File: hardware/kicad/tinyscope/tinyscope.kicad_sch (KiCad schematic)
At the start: 44 parts, among them J1 USB_C_Receptacle_USB2.0, J2 Conn_01x02, J3 Conn_01x02, Q1 PMOS, U1 USBLC6-2SC6_MOD, U2 BQ24075RGT, U3 MAX17048G, U4 TPS54360DDA

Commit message: feat: hardware: Add tinyscope kicad project. Adds TPS62133 3V3 buck converter
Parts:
- added C13: 100n, symbol Device:C_Small
- added C14: 10u, symbol Device:C_Small
- added C15: 3n3, symbol Device:C_Small
- added C16: 22u, symbol Device:C_Small
- added L2: 2u2, symbol Device:L_Small
- added R16: 100k, symbol Device:R_Small
- added R17: 31k8, symbol Device:R_Small
- added R18: 10k2, symbol Device:R_Small
- added U5: TPS62133, Package_DFN_QFN:VQFN-16-1EP_3x3mm_P0.5mm_EP1.68x1.68mm_ThermalVias, symbol Regulator_Switching:TPS62133
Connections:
- net BQ24075_OUT: now also C14.1, U5.11 (PVIN), U5.12 (PVIN)
- net GND: now also C13.2, C14.2, C15.1, C16.2, R18.2, U5.15 (PGND), U5.16 (PGND), U5.17 (EP), U5.6 (AGND), U5.7 (FSW), U5.8 (DEF)
- new net: R17.2, R18.1, U5.5 (FB)
- new net: L2.1, U5.1 (SW), U5.2 (SW), U5.3 (SW)
- new net: C13.1, U5.10 (AVIN), U5.13 (EN)
- new net: L2.2, R16.1, U5.14 (VOS)
- new net: C15.2, U5.9 (SS/TR)
- new net +3V3: C16.1, R16.2, R17.1, U5.4 (PG)

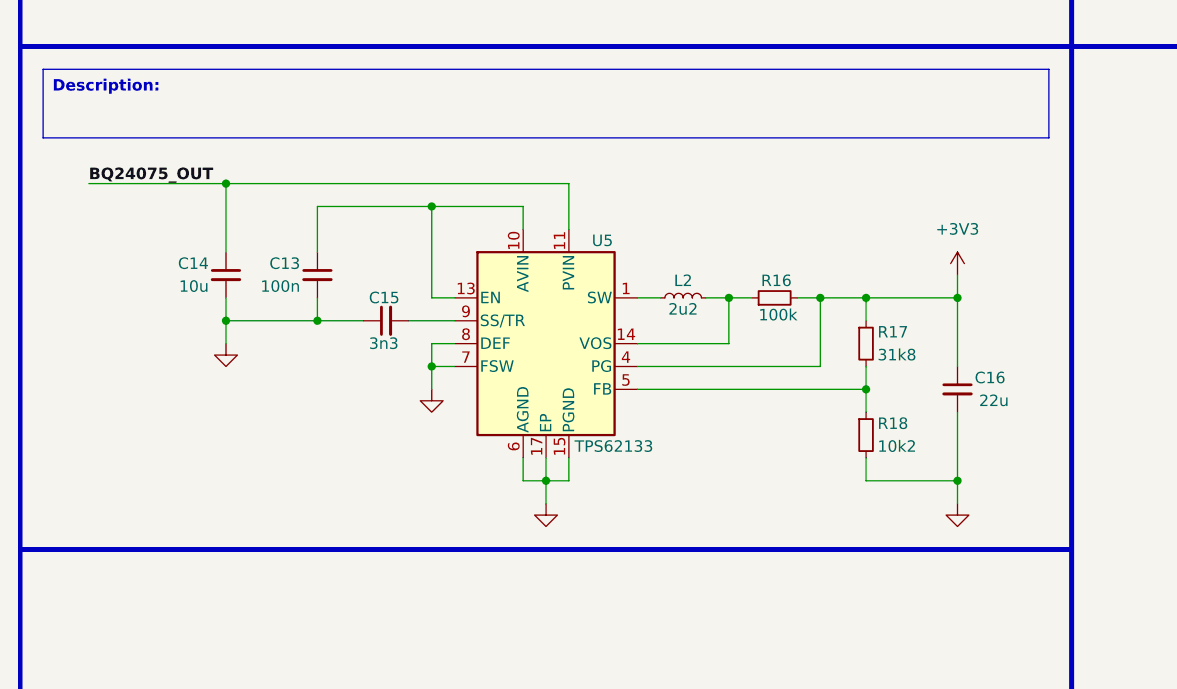
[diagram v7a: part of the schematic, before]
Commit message: feat: hardware: Add tinyscope kicad project. Adds TPS63802 3V3 buck-boost converter instead of the previous one
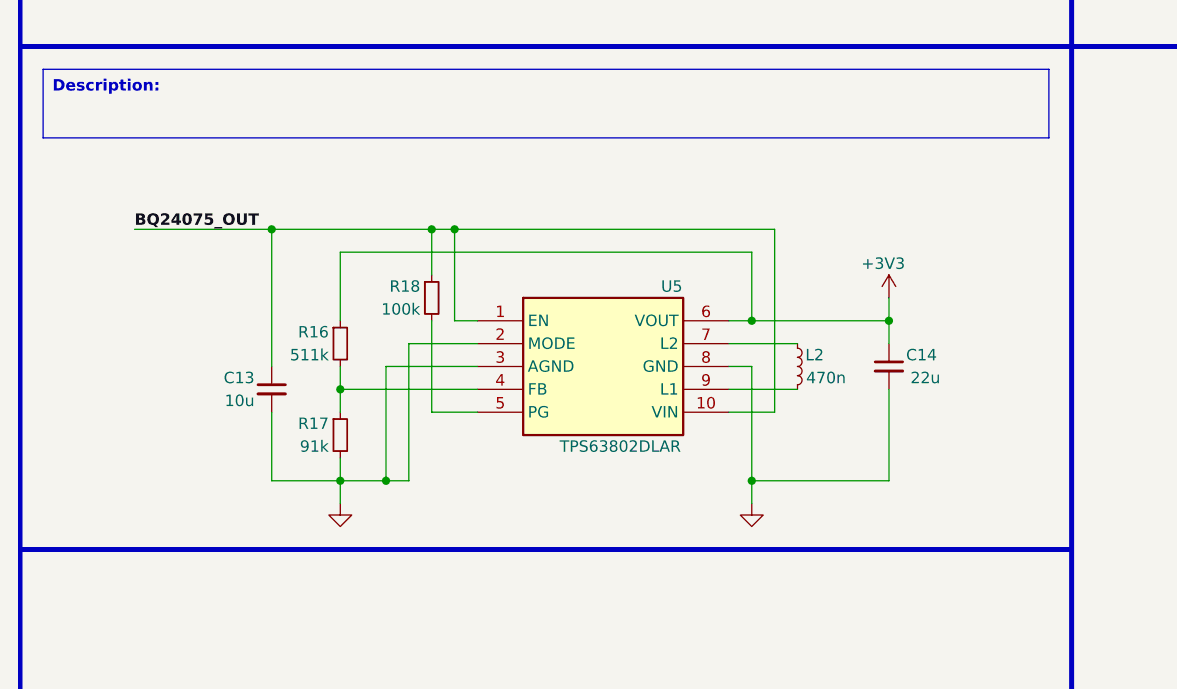
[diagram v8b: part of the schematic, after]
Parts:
- removed C15: 3n3, symbol Device:C_Small
- removed C16: 22u, symbol Device:C_Small
- removed U5: TPS62133, Package_DFN_QFN:VQFN-16-1EP_3x3mm_P0.5mm_EP1.68x1.68mm_ThermalVias, symbol Regulator_Switching:TPS62133
- added U5: TPS63802DLAR, TPS63802DLAR, symbol TPS63802DLAR:TPS63802DLAR
- C13: value 100n -> 10u
- C14: value 10u -> 22u
- L2: value 2u2 -> 470n
- R16: value 100k -> 511k
- R17: value 31k8 -> 91k
- R18: value 10k2 -> 100k
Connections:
- net +3V3: now also C14.1, R16.1, U5.6 (VOUT); no longer R16.2, R17.1
- net BQ24075_OUT: now also C13.1, R18.1, U5.1 (EN), U5.10 (VIN); no longer C14.1
- net GND: now also R17.2, U5.2 (MODE), U5.3 (AGND), U5.8 (GND); no longer R18.2
- net at L2.1: now also U5.7 (L2)
- net at L2.2: now also U5.9 (L1); no longer R16.1
- new net: R16.2, R17.1, U5.4 (FB)
- new net: R18.2, U5.5 (PG)
